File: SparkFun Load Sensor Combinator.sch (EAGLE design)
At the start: 14 parts

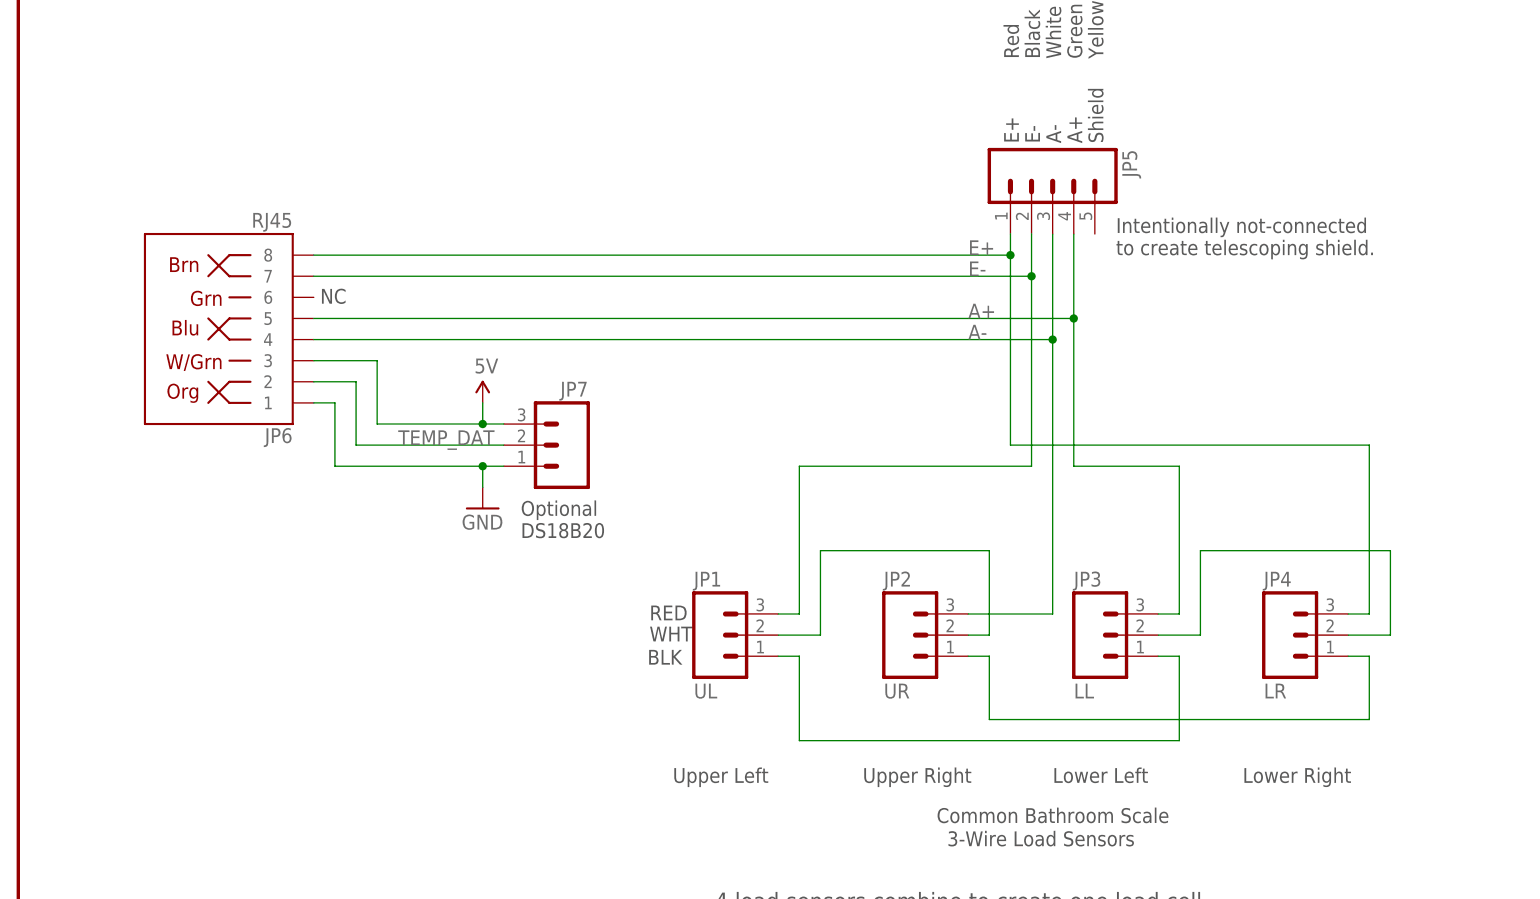
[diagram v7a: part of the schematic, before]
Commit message: Changed silk from BLK to -, WHT to C.
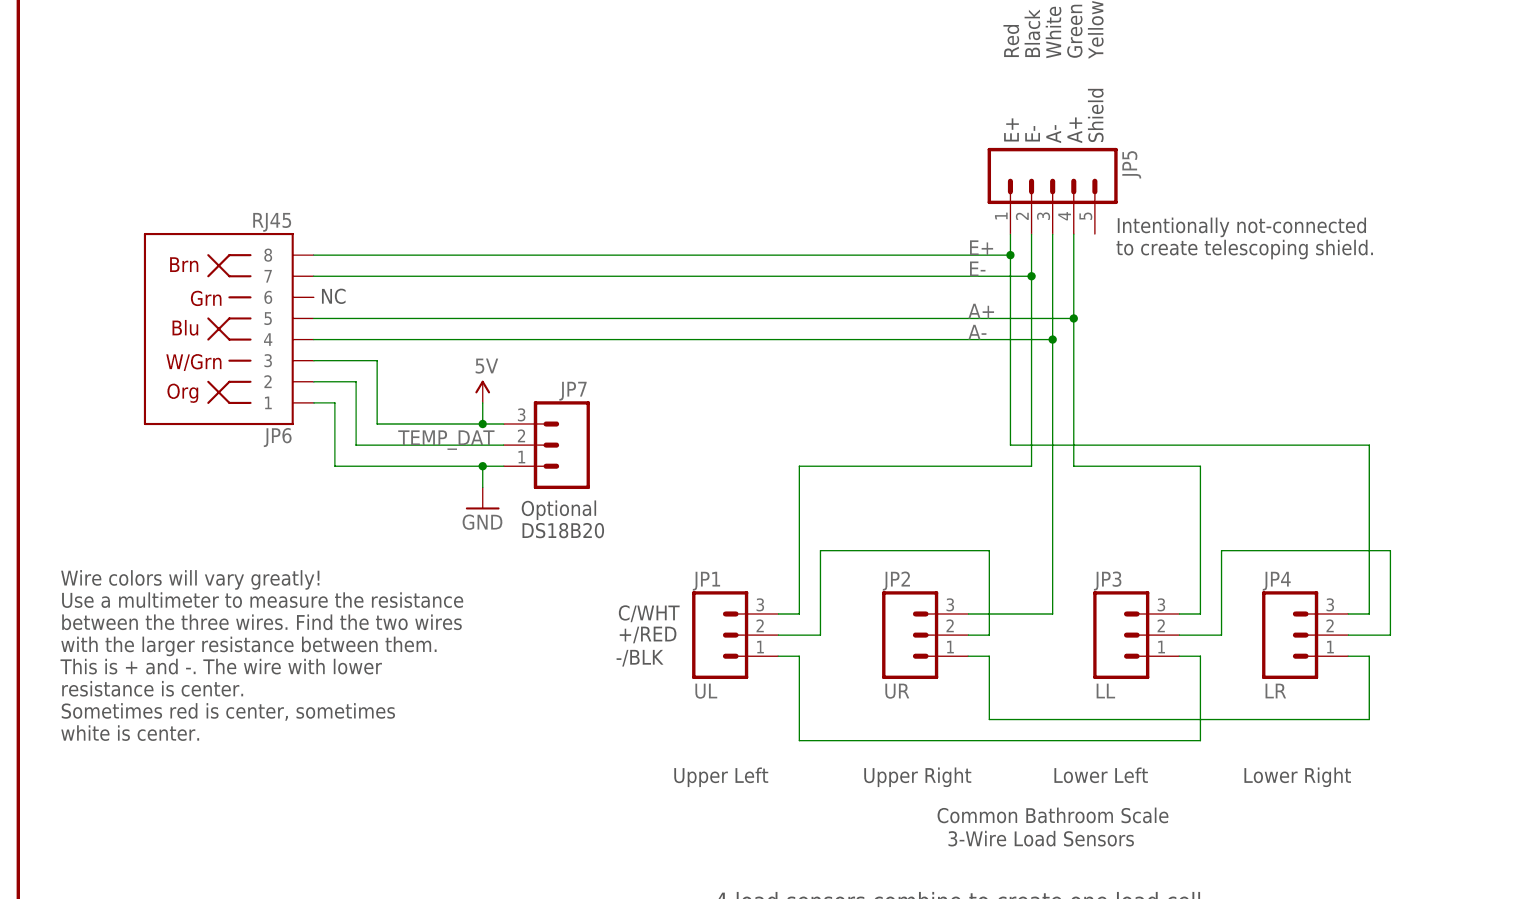
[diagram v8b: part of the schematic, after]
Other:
- note added: "+/RED"
- note added: "-/BLK"
- note added: "C/WHT"
- note added: "Wire colors will vary greatly\! Use a multimeter to measure the resistance between the three wires. Find the two wires with the larger resistance between them. This is + and -. The wire with lower resistance is center. Sometimes red is center, sometimes white is center."
- note removed: "BLK"
- note removed: "RED"
- note removed: "WHT"
- moved on the sheet: JP3
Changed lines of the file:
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@@
 <?xml version="1.0" encoding="utf-8"?>
 <!DOCTYPE eagle SYSTEM "eagle.dtd">
-<eagle version="7.2.0">
+<eagle version="7.1.0">
 <drawing>
 <settings>
@@
 <text x="120.396" y="155.702" size="1.778" layer="97" rot="R90">Red</text>
 <text x="122.936" y="155.702" size="1.778" layer="97" rot="R90">Black</text>
-<text x="125.476" y="155.702" size="1.778" layer="97" rot="R90">White</text>
-<text x="128.016" y="155.702" size="1.778" layer="97" rot="R90">Green</text>
 <text x="147.32" y="68.58" size="1.778" layer="97">Lower Right</text>
 <text x="101.6" y="68.58" size="1.778" layer="97">Upper Right</text>
@@
 <text x="110.49" y="63.754" size="1.778" layer="97">Common Bathroom Scale</text>
 <text x="104.394" y="168.656" size="1.778" layer="97">Connections to Amplifier</text>
-<text x="75.692" y="82.804" size="1.778" layer="97">BLK</text>
-<text x="75.946" y="85.598" size="1.778" layer="97">WHT</text>
-<text x="75.946" y="88.138" size="1.778" layer="97">RED</text>
+<text x="71.882" y="82.804" size="1.778" layer="97">-/BLK</text>
+<text x="72.136" y="88.138" size="1.778" layer="97">C/WHT</text>
+<text x="72.136" y="85.598" size="1.778" layer="97">+/RED</text>
 <text x="83.82" y="53.34" size="2.032" layer="97">4 load sensors combine to create one load cell</text>
 <text x="130.556" y="145.542" size="1.778" layer="97" rot="R90">Shield</text>
@@
 <text x="170.942" y="11.43" size="2.54" layer="94">N. Seidle</text>
 <text x="238.76" y="7.62" size="2.54" layer="94">v10</text>
+<text x="125.476" y="155.702" size="1.778" layer="97" rot="R90">White</text>
+<text x="128.016" y="155.702" size="1.778" layer="97" rot="R90">Green</text>
+<text x="5.08" y="73.66" size="1.778" layer="97">Wire colors will vary greatly\!
+Use a multimeter to measure the resistance
+between the three wires. Find the two wires
+with the larger resistance between them.
+This is + and -. The wire with lower
+resistance is center.
+Sometimes red is center, sometimes
+white is center.</text>
 </plain>
 <instances>
@@
 <instance part="JP1" gate="G$1" x="83.82" y="86.36"/>
 <instance part="JP2" gate="G$1" x="106.68" y="86.36"/>
-<instance part="JP3" gate="G$1" x="129.54" y="86.36"/>
+<instance part="JP3" gate="G$1" x="132.08" y="86.36"/>
 <instance part="JP4" gate="G$1" x="152.4" y="86.36"/>
 <instance part="FRAME1" gate="G$1" x="0" y="0">
@@
 </instance>
 <instance part="FRAME1" gate="V" x="147.32" y="0"/>
-<instance part="JP5" gate="G$1" x="124.46" y="142.24" rot="R270"/>
+<instance part="JP5" gate="G$1" x="124.46" y="142.24" smashed="yes" rot="R270">
+<attribute name="VALUE" x="114.3" y="144.78" size="1.778" layer="96" rot="R270"/>
+<attribute name="NAME" x="132.842" y="144.78" size="1.778" layer="95" rot="R270"/>
+</instance>
 <instance part="JP6" gate="JP1" x="27.94" y="121.92" rot="R180"/>
 <instance part="JP7" gate="G$1" x="66.04" y="109.22" rot="MR0"/>
@@
 <segment>
 <pinref part="JP3" gate="G$1" pin="1"/>
-<wire x1="137.16" y1="83.82" x2="139.7" y2="83.82" width="0.1524" layer="91"/>
-<wire x1="139.7" y1="83.82" x2="139.7" y2="73.66" width="0.1524" layer="91"/>
-<wire x1="139.7" y1="73.66" x2="93.98" y2="73.66" width="0.1524" layer="91"/>
+<wire x1="139.7" y1="83.82" x2="142.24" y2="83.82" width="0.1524" layer="91"/>
+<wire x1="142.24" y1="83.82" x2="142.24" y2="73.66" width="0.1524" layer="91"/>
+<wire x1="142.24" y1="73.66" x2="93.98" y2="73.66" width="0.1524" layer="91"/>
 <wire x1="93.98" y1="73.66" x2="93.98" y2="83.82" width="0.1524" layer="91"/>
 <pinref part="JP1" gate="G$1" pin="1"/>
@@
 <wire x1="160.02" y1="86.36" x2="165.1" y2="86.36" width="0.1524" layer="91"/>
 <wire x1="165.1" y1="86.36" x2="165.1" y2="96.52" width="0.1524" layer="91"/>
-<wire x1="165.1" y1="96.52" x2="142.24" y2="96.52" width="0.1524" layer="91"/>
-<wire x1="142.24" y1="96.52" x2="142.24" y2="86.36" width="0.1524" layer="91"/>
+<wire x1="165.1" y1="96.52" x2="144.78" y2="96.52" width="0.1524" layer="91"/>
+<wire x1="144.78" y1="96.52" x2="144.78" y2="86.36" width="0.1524" layer="91"/>
 <pinref part="JP3" gate="G$1" pin="2"/>
-<wire x1="142.24" y1="86.36" x2="137.16" y2="86.36" width="0.1524" layer="91"/>
+<wire x1="144.78" y1="86.36" x2="139.7" y2="86.36" width="0.1524" layer="91"/>
 </segment>
 </net>
@@
 <net name="A+" class="0">
 <segment>
-<wire x1="127" y1="106.68" x2="139.7" y2="106.68" width="0.1524" layer="91"/>
-<wire x1="139.7" y1="106.68" x2="139.7" y2="88.9" width="0.1524" layer="91"/>
+<wire x1="127" y1="106.68" x2="142.24" y2="106.68" width="0.1524" layer="91"/>
+<wire x1="142.24" y1="106.68" x2="142.24" y2="88.9" width="0.1524" layer="91"/>
 <pinref part="JP3" gate="G$1" pin="3"/>
-<wire x1="139.7" y1="88.9" x2="137.16" y2="88.9" width="0.1524" layer="91"/>
+<wire x1="142.24" y1="88.9" x2="139.7" y2="88.9" width="0.1524" layer="91"/>
 <wire x1="127" y1="106.68" x2="127" y2="124.46" width="0.1524" layer="91"/>
 <wire x1="127" y1="124.46" x2="35.56" y2="124.46" width="0.1524" layer="91"/>
